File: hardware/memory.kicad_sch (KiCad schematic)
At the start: 0 parts

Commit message: Emulated memory: rewrite architecture, add local-bus/register sheet
- docs/v3-architecture.md: RP2350B serves DCK/ROM images from internal SRAM
  via PIO+DMA; no flash or SRAM chips; 8-bit multiplexed local bus; slot map
  file replaces fixed flash banks; ESP32-C3-WROOM-02 for Zimodem.
- memory sheet: 74LVC257 address byte muxes, ALO/AHI/CTL/STAT registers,
  74LVC139 select, power-on clear for CTL.
- interface sheet: 74LVC06 inverting open-drain drivers with active-high
  requests (safe power-up state), RESET_HOLD pull-up, address transceivers
  always enabled, MA8-MA15 to the muxes, WIFI_DL inverter.
- ERC: only cross-sheet labels/inputs pending the MCU and peripheral sheets.

Co-Authored-By: Claude Fable 5.1 <noreply@anthropic.com>
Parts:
- added C10, C11, C12, C13, C14, C15, C16: 100n, Capacitor_SMD:C_0603_1608Metric, symbol Device:C
- added C9: 1u, Capacitor_SMD:C_0603_1608Metric, symbol Device:C
- added D1: BAT54, Diode_SMD:D_SOD-123, symbol Device:D_Schottky
- added R4: 10k, Resistor_SMD:R_0603_1608Metric, symbol Device:R
- added U10, U11: 74LVC257APW, Package_SO:TSSOP-16_4.4x5mm_P0.65mm, symbol 74xx:74LS257
- added U12, U13: 74LVC574APW, Package_SO:TSSOP-20_4.4x6.5mm_P0.65mm, symbol 74xx:74LS574
- added U14: 74LVC273APW, Package_SO:TSSOP-20_4.4x6.5mm_P0.65mm, symbol 74xx:74LS273
- added U15: 74LVC541APW, Package_SO:TSSOP-20_4.4x6.5mm_P0.65mm, symbol 74xx:74LS541
- added U16: 74LVC139APW, Package_SO:TSSOP-16_4.4x5mm_P0.65mm, symbol 74xx:74LS139
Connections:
- new net +3V3: C10.1, C11.1, C12.1, C13.1, C14.1, C15.1, C16.1, D1.2 (A), R4.1, U10.16 (VCC), U11.16 (VCC), U12.20 (VCC), U13.20 (VCC), U14.20 (VCC), U15.20 (VCC), U16.15 (E), U16.16 (VCC)
- new net ASEL: U10.1 (S), U11.1 (S)
- new net BUSRQ: U14.5 (Q1)
- new net DMA_EN: U14.2 (Q0)
- new net GND: C10.2, C11.2, C12.2, C13.2, C14.2, C15.2, C16.2, C9.2, U10.8 (GND), U11.8 (GND), U12.10 (GND), U13.10 (GND), U14.10 (GND), U15.10 (GND), U15.19 (G2), U16.13 (A1), U16.14 (A0), U16.8 (GND)
- new net JOY_DOWN: U15.3 (A1)
- new net JOY_FIRE1: U15.6 (A4)
- new net JOY_FIRE2: U15.7 (A5)
- new net JOY_LEFT: U15.4 (A2)
- new net JOY_RIGHT: U15.5 (A3)
- new net JOY_UP: U15.2 (A0)
- new net LED: U14.16 (Q6)
- new net MA0: U10.2 (I0a), U12.19 (Q0)
- new net MA1: U10.5 (I0b), U12.18 (Q1)
- new net MA10: U10.13 (I1c), U13.17 (Q2)
- new net MA11: U10.10 (I1d), U13.16 (Q3)
- new net MA12: U11.3 (I1a), U13.15 (Q4)
- new net MA13: U11.6 (I1b), U13.14 (Q5)
- new net MA14: U11.13 (I1c), U13.13 (Q6)
- new net MA15: U11.10 (I1d), U13.12 (Q7)
- new net MA2: U10.14 (I0c), U12.17 (Q2)
- new net MA3: U10.11 (I0d), U12.16 (Q3)
- new net MA4: U11.2 (I0a), U12.15 (Q4)
- new net MA5: U11.5 (I0b), U12.14 (Q5)
- new net MA6: U11.14 (I0c), U12.13 (Q6)
- new net MA7: U11.11 (I0d), U12.12 (Q7)
- new net MA8: U10.3 (I1a), U13.19 (Q0)
- new net MA9: U10.6 (I1b), U13.18 (Q1)
- new net MD0: U10.4 (Za), U12.2 (D0), U13.2 (D0), U14.3 (D0), U15.18 (Y0)
- new net MD1: U10.7 (Zb), U12.3 (D1), U13.3 (D1), U14.4 (D1), U15.17 (Y1)
- new net MD2: U10.12 (Zc), U12.4 (D2), U13.4 (D2), U14.7 (D2), U15.16 (Y2)
- new net MD3: U10.9 (Zd), U12.5 (D3), U13.5 (D3), U14.8 (D3), U15.15 (Y3)
- new net MD4: U11.4 (Za), U12.6 (D4), U13.6 (D4), U14.13 (D4), U15.14 (Y4)
- new net MD5: U11.7 (Zb), U12.7 (D5), U13.7 (D5), U14.14 (D5), U15.13 (Y5)
- new net MD6: U11.12 (Zc), U12.8 (D6), U13.8 (D6), U14.17 (D6), U15.12 (Y6)
- new net MD7: U11.9 (Zd), U12.9 (D7), U13.9 (D7), U14.18 (D7), U15.11 (Y7)
- new net NMI_REQ: U14.6 (Q2)
- new net REG_SEL0: U16.2 (A0)
- new net REG_SEL1: U16.3 (A1)
- new net SD_CD: U15.9 (A7)
- new net WIFI_DL: U14.15 (Q5)
- new net WIFI_EN: U14.12 (Q4)
- new net nAOE: U10.15 (OE), U11.15 (OE)
- new net nBUSAK: U15.8 (A6)
- new net nDMA_EN: U12.1 (OE), U13.1 (OE)
- new net nOLED_RST: U14.9 (Q3)
- new net nPOR: C9.1, D1.1 (K), R4.2, U14.1 (~{Mr})
- new net nRD_STAT: U15.1 (G1), U16.7 (O3)
- new net nREG_STB: U16.1 (E)
- new net nWR_AHI: U13.11 (Cp), U16.5 (O1)
- new net nWR_ALO: U12.11 (Cp), U16.4 (O0)
- new net nWR_CTL: U14.11 (Cp), U16.6 (O2)
- no-connect marks 0 -> 5
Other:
- note added: "Local bus MD0-MD7 carries the Z80 address (two bytes through U10/U11), the Z80 data (interface sheet U3) and the registers."
- note added: "No flash or SRAM: the RP2350B serves memory from internal SRAM (PIO + DMA). ALO/AHI drive MA only in DMA mode."
- note added: "R4/C9/D1: ~10 ms power-on clear of CTL,"
- note added: "so all control bits start at 0."
- note removed: "Flash (TSOP-32), SRAM (SOP-32), ALO/AHI/CTL/STAT registers, 74LVC139, 74LVC157, 74LVC125 DMA drivers"
- title: TS-Pico v3: Memory Bus -> TS-Pico v3: Local Bus and Registers

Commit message: Remaining sheets: power, SD and display, WiFi, audio, joystick; ERC clean
- Power: Schottky diode-OR of edge +5V and USB VBUS (card runs from the
  2068/expansion bus, USB alone, or both), two TLV1117LV33 LDOs, bulk caps
- SD: Hirose DM3AT in SPI mode with series R, pull-ups, card detect to STAT
- OLED: 7-pin header (Waveshare 1.27in 128x96 SSD1351) on SPI1
- WiFi: ESP32-C3-WROOM-02 on UART, EN/boot from CTL, IO8 pull-up
- Audio: PWM low-pass, 2068 SOUND mix, MCP6002 buffers, 3.5 mm jack
- Joystick: DE-9 Kempston with pull-ups, series R, optional +5V jumper
- Memory sheet: activity LED on CTL bit 6
- Docs: power decision updated

Co-Authored-By: Claude Fable 5.1 <noreply@anthropic.com>
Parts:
- added D4: green, LED_SMD:LED_0603_1608Metric, symbol Device:LED
- added R5: 1k, Resistor_SMD:R_0603_1608Metric, symbol Device:R
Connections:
- net GND: now also D4.1 (K)
- net LED: now also R5.1
- new net LED_K: D4.2 (A), R5.2
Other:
- note added: "R5/D4: activity LED, CTL bit 6."
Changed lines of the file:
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@@
   (text "R4/C9/D1: ~10 ms power-on clear of CTL," (exclude_from_sim no) (at 355 118 0) (effects (font (size 1.5 1.5)) (justify left bottom)))
   (text "so all control bits start at 0." (exclude_from_sim no) (at 355 121 0) (effects (font (size 1.5 1.5)) (justify left bottom)))
+  (symbol (lib_id "Device:R") (at 369.57 160.02 0) (unit 1)
+    (exclude_from_sim no) (in_bom yes) (on_board yes) (dnp no)
+    (property "Reference" "R5" (at 372.57 151.71 0) (effects (font (size 1.27 1.27)) (justify left)))
+    (property "Value" "1k" (at 372.57 154.21 0) (effects (font (size 1.27 1.27)) (justify left)))
+    (property "Footprint" "Resistor_SMD:R_0603_1608Metric" (at 369.57 160.02 0) (effects (font (size 1.27 1.27)) (justify left) (hide yes)))
+    (property "Datasheet" "" (at 369.57 160.02 0) (effects (font (size 1.27 1.27)) (justify left) (hide yes)))
+    (property "Description" "" (at 369.57 160.02 0) (effects (font (size 1.27 1.27)) (justify left) (hide yes)))
+    (pin "1")
+    (pin "2")
+    (instances (project "tspico-v3" (path "/9088d141-8624-4d5c-91a9-7a3a7a90b3cc/e99fe9a8-9037-4040-a342-12a0ddc42052" (reference "R5") (unit 1))))
+  )
+  (global_label "LED" (shape input) (at 369.57 156.21 90) (effects (font (size 1.27 1.27)) (justify left)))
+  (label "LED_K" (at 369.57 163.83 270) (effects (font (size 1.27 1.27)) (justify right bottom)))
+  (symbol (lib_id "Device:LED") (at 374.65 180.34 0) (unit 1)
+    (exclude_from_sim no) (in_bom yes) (on_board yes) (dnp no)
+    (property "Reference" "D4" (at 377.65 173.3 0) (effects (font (size 1.27 1.27)) (justify left)))
+    (property "Value" "green" (at 377.65 175.8 0) (effects (font (size 1.27 1.27)) (justify left)))
+    (property "Footprint" "LED_SMD:LED_0603_1608Metric" (at 374.65 180.34 0) (effects (font (size 1.27 1.27)) (justify left) (hide yes)))
+    (property "Datasheet" "" (at 374.65 180.34 0) (effects (font (size 1.27 1.27)) (justify left) (hide yes)))
+    (property "Description" "" (at 374.65 180.34 0) (effects (font (size 1.27 1.27)) (justify left) (hide yes)))
+    (pin "1")
+    (pin "2")
+    (instances (project "tspico-v3" (path "/9088d141-8624-4d5c-91a9-7a3a7a90b3cc/e99fe9a8-9037-4040-a342-12a0ddc42052" (reference "D4") (unit 1))))
+  )
+  (label "LED_K" (at 378.46 180.34 0) (effects (font (size 1.27 1.27)) (justify left bottom)))
+  (label "GND" (at 370.84 180.34 180) (effects (font (size 1.27 1.27)) (justify right bottom)))
+  (text "R5/D4: activity LED, CTL bit 6." (exclude_from_sim no) (at 355 195 0) (effects (font (size 1.5 1.5)) (justify left bottom)))
   (symbol (lib_id "Device:C") (at 39.37 255.27 0) (unit 1)
     (exclude_from_sim no) (in_bom yes) (on_board yes) (dnp no)

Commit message: BOM pass: LCSC and MPN fields on every part, JLCPCB BOM export
- scripts/parts.py: part table looked up 2026-09-16; schlib stamps fields
- substitutions for stock: 74HC273PW, 74LVC139PW, TI LVC04/08/126/574/1G86,
  33R USB series, XKB TS-1187A switches, Panasonic polymer 220uF, B5819W
- bom/: JLCPCB-format and full BOM CSVs

Co-Authored-By: Claude Fable 5.1 <noreply@anthropic.com>
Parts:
- C10, C11, C12, C13, C14, C15, C16: LCSC (none) -> C14663; MPN (none) -> CC0603KRX7R9BB104
- C9: LCSC (none) -> C15849; MPN (none) -> CL10A105KB8NNNC
- D1: value BAT54 -> B5819W; LCSC (none) -> C8598; MPN (none) -> B5819W SL
- D4: LCSC (none) -> C72043; MPN (none) -> 19-217/GHC-YR1S2/3T
- R4: LCSC (none) -> C25804; MPN (none) -> 0603WAF1002T5E
- R5: LCSC (none) -> C21190; MPN (none) -> 0603WAF1001T5E
- U10, U11: LCSC (none) -> C6083; MPN (none) -> 74LVC257APW,118
- U12, U13: LCSC (none) -> C7672; MPN (none) -> SN74LVC574APWR
- U14: value 74LVC273APW -> 74HC273PW; LCSC (none) -> C131680; MPN (none) -> 74HC273PW,118
- U15: LCSC (none) -> C6093; MPN (none) -> 74LVC541APW,118
- U16: value 74LVC139APW -> 74LVC139PW; LCSC (none) -> C6064; MPN (none) -> 74LVC139PW,118

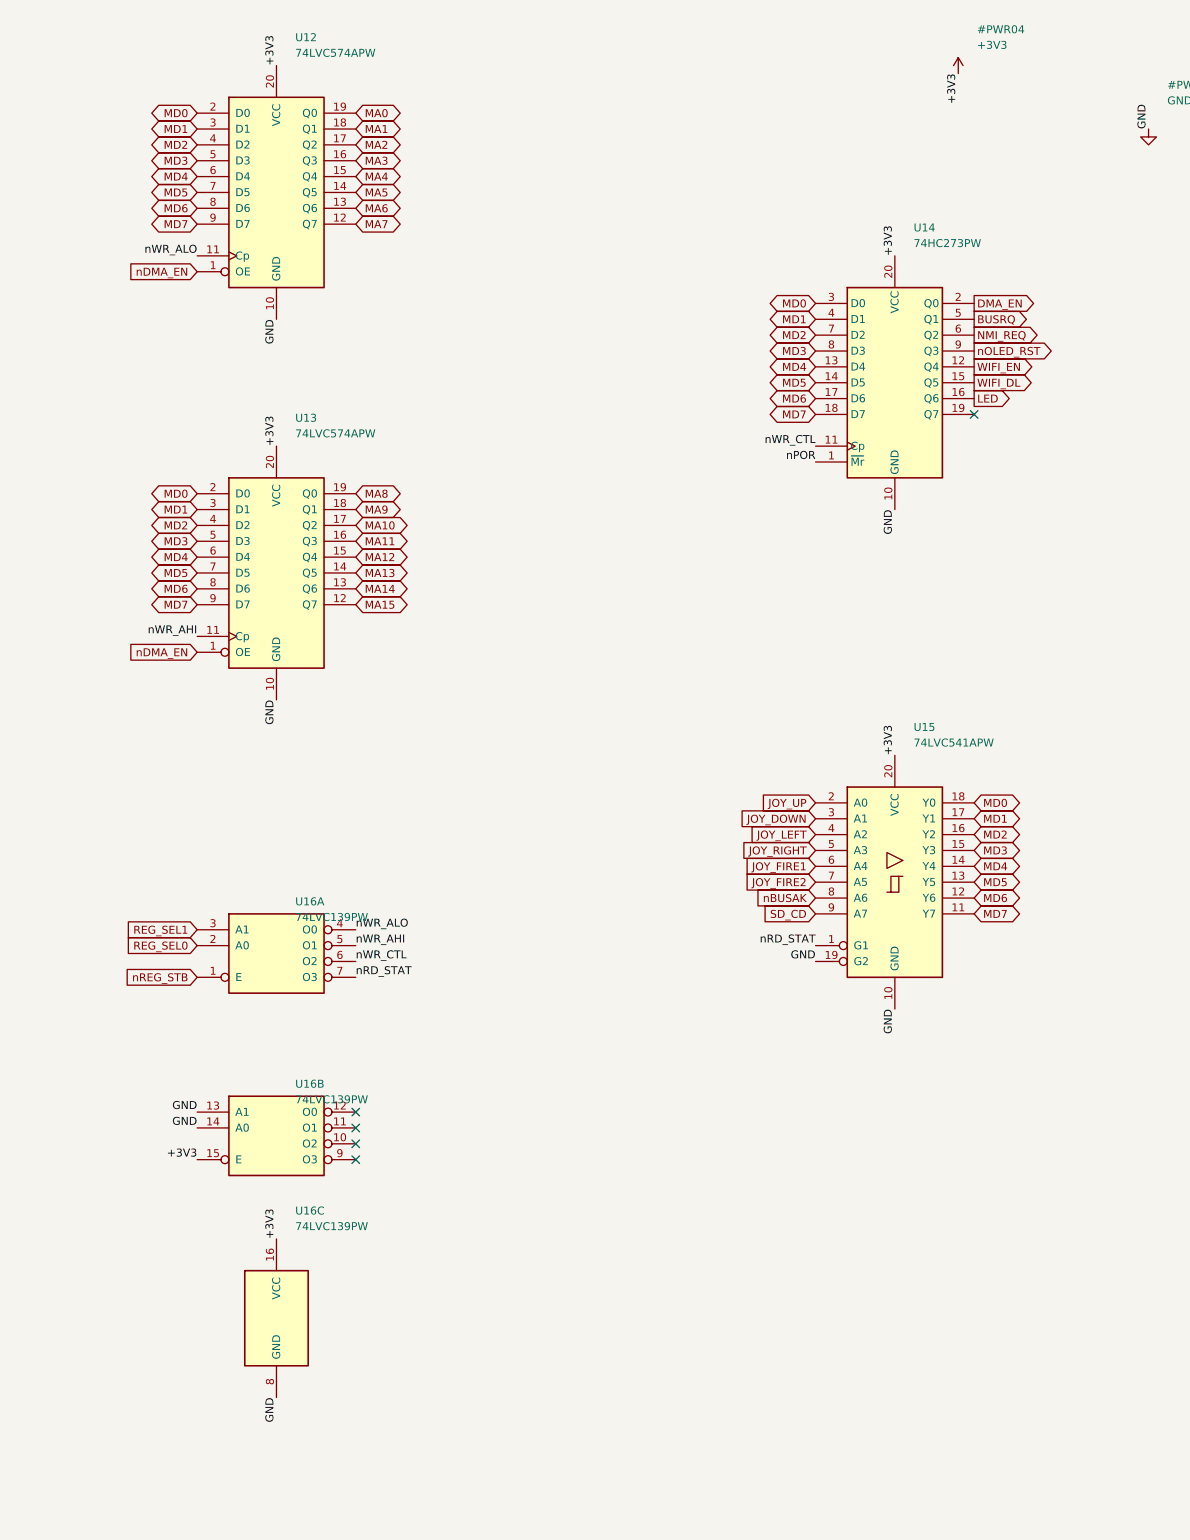
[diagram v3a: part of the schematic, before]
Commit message: BOM cost optimisation against the JLCPCB catalog; schematic-side regulator fix
jlc_price.py prices the BOM via JLCPCB's parts API. Substitutions cut parts+fees
per board from $32.95 to $17.19 on a 10-board run: PSRAM DNP, electrolytic bulk
caps, TF-01A socket, PJ-320D jack, 74HC574, GD25Q128E, 0603 10 uF, basic LED,
preferred MCP6002; U16 decoder deleted (strobes on GPIO), U8 and U15 become
74LVC245s; J3/J5 hand-soldered. Adds the AOTA inductor and VREG_AVDD filter.
PCB needs a relayout; fab/ is stale.

Co-Authored-By: Claude Fable 5.1 <noreply@anthropic.com>
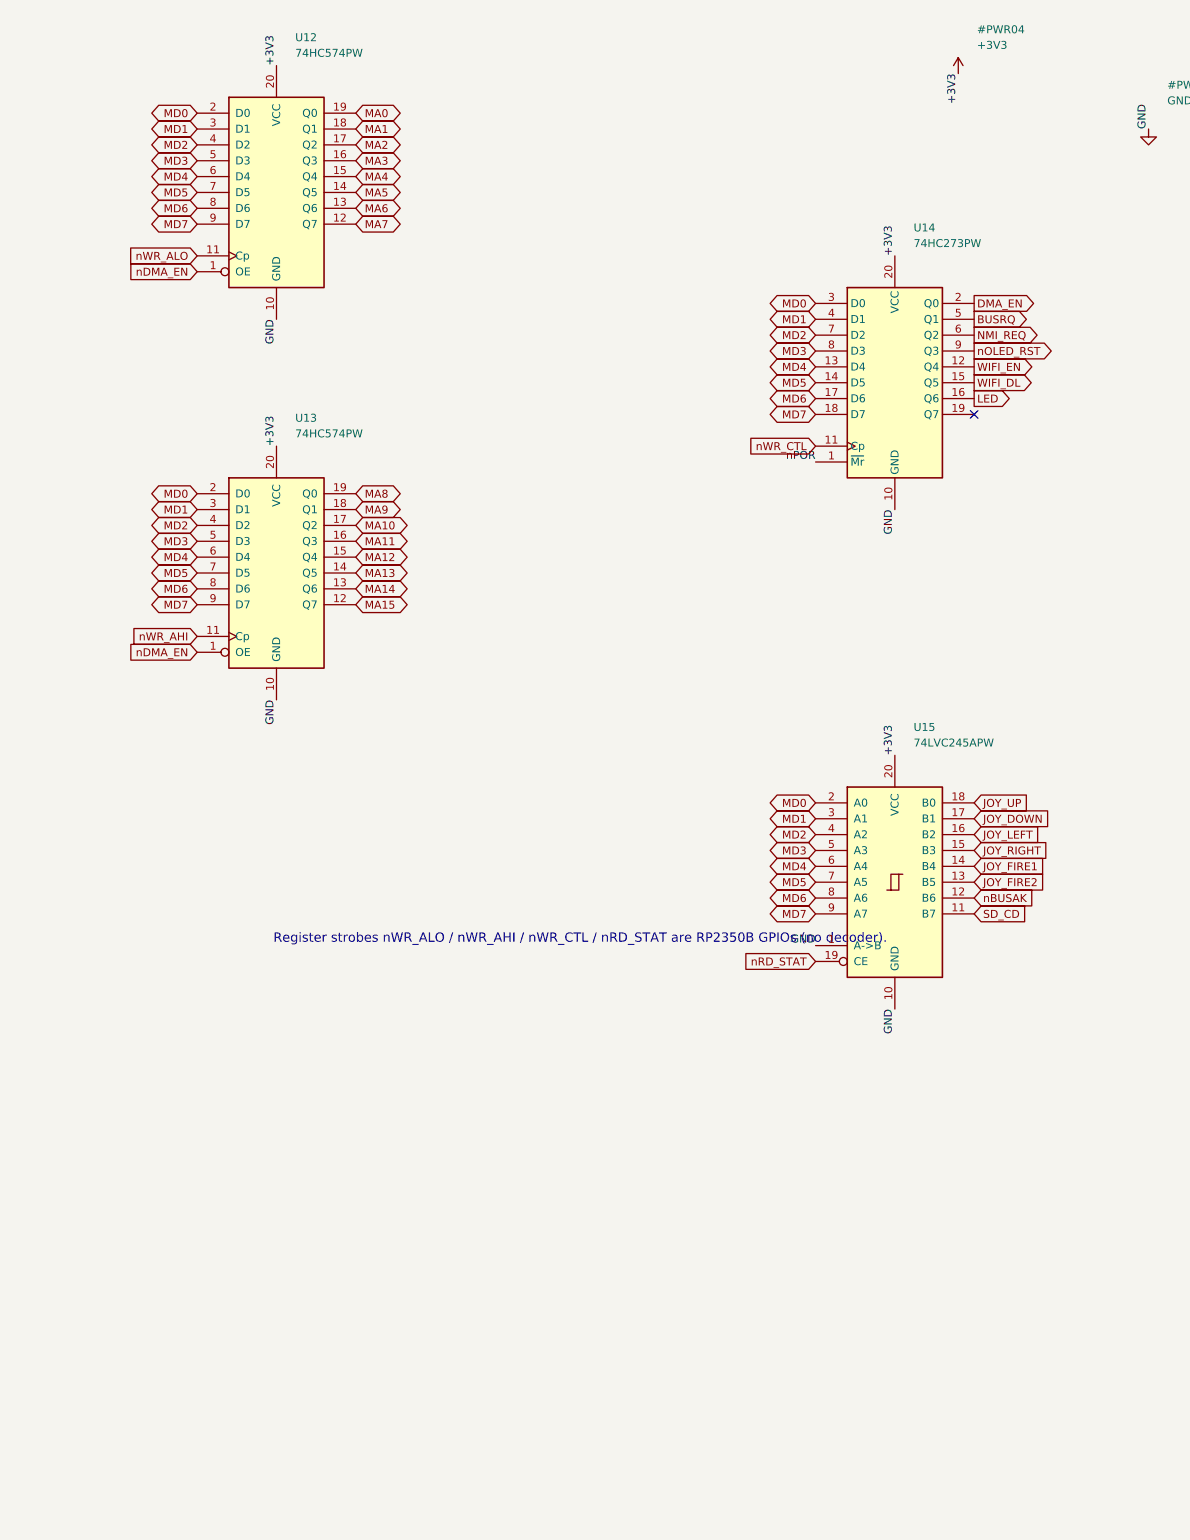
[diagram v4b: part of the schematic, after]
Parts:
- removed U15: 74LVC541APW, Package_SO:TSSOP-20_4.4x6.5mm_P0.65mm, symbol 74xx:74LS541
- removed U16: 74LVC139PW, Package_SO:TSSOP-16_4.4x5mm_P0.65mm, symbol 74xx:74LS139
- added U15: 74LVC245APW, Package_SO:TSSOP-20_4.4x6.5mm_P0.65mm, symbol 74xx:74LS245
- D4: footprint LED_SMD:LED_0603_1608Metric -> LED_SMD:LED_0805_2012Metric; LCSC C72043 -> C2297; MPN 19-217/GHC-YR1S2/3T -> KT-0805G
- U10, U11: LCSC C6083 -> C205921; MPN 74LVC257APW,118 -> SN74LVC257APWR
- U12, U13: value 74LVC574APW -> 74HC574PW; LCSC C7672 -> C54796860; MPN SN74LVC574APWR -> 74HC574PW
- U14: LCSC C131680 -> C44512760; MPN 74HC273PW,118 -> SN74HC273PWR-JSM
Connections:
- net +3V3: now also U15.20 (VCC)
- net GND: now also U15.1 (A->B), U15.10 (GND)
- net JOY_DOWN: now also U15.17 (B1)
- net JOY_FIRE1: now also U15.14 (B4)
- net JOY_FIRE2: now also U15.13 (B5)
- net JOY_LEFT: now also U15.16 (B2)
- net JOY_RIGHT: now also U15.15 (B3)
- net JOY_UP: now also U15.18 (B0)
- net MD0: now also U15.2 (A0)
- net MD1: now also U15.3 (A1)
- net MD2: now also U15.4 (A2)
- net MD3: now also U15.5 (A3)
- net MD4: now also U15.6 (A4)
- net MD5: now also U15.7 (A5)
- net MD6: now also U15.8 (A6)
- net MD7: now also U15.9 (A7)
- net SD_CD: now also U15.11 (B7)
- net nBUSAK: now also U15.12 (B6)
- net nRD_STAT: now also U15.19 (CE)
- no-connect marks 5 -> 1
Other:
- note added: "Register strobes nWR_ALO / nWR_AHI / nWR_CTL / nRD_STAT are RP2350B GPIOs (no decoder)."

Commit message: Logic consolidation: 15 packages to 8 fitted
Address buffers' output enables replace the 74LVC257 byte muxes and the MA bus;
one 74LVC32 makes MEMRD/MEMWR/IORD/IOWR strobes (replaces the 04 and 08);
XL9555 I2C expander replaces the CTL register, its power-on clear and the STAT
buffer; DMA parts are a DNP stuffing option (config.DMA_OPTION), with 74LVC574
latches directly on the address bus. GPIO map, architecture doc and cost notes
updated. Parts + fees per board now $14.93 on a 10-board run.

Co-Authored-By: Claude Fable 5.1 <noreply@anthropic.com>
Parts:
- removed C11, C12, C13, C14, C15, C16: 100n, Capacitor_SMD:C_0603_1608Metric, symbol Device:C
- removed C9: 1u, Capacitor_SMD:C_0603_1608Metric, symbol Device:C
- removed D1: B5819W, Diode_SMD:D_SOD-123, symbol Device:D_Schottky
- removed R4: 10k, Resistor_SMD:R_0603_1608Metric, symbol Device:R
- removed U10, U11: 74LVC257APW, Package_SO:TSSOP-16_4.4x5mm_P0.65mm, symbol 74xx:74LS257
- removed U12, U13: 74HC574PW, Package_SO:TSSOP-20_4.4x6.5mm_P0.65mm, symbol 74xx:74LS574
- removed U14: 74HC273PW, Package_SO:TSSOP-20_4.4x6.5mm_P0.65mm, symbol 74xx:74LS273
- removed U15: 74LVC245APW, Package_SO:TSSOP-20_4.4x6.5mm_P0.65mm, symbol 74xx:74LS245
- added R10, R11, R12, R13, R8, R9: 10k, Resistor_SMD:R_0603_1608Metric, symbol Device:R
- added R6, R7: 4k7, Resistor_SMD:R_0603_1608Metric, symbol Device:R
- added U15: XL9555, Package_SO:TSSOP-24_4.4x7.8mm_P0.65mm, symbol Interface_Expansion:PCA9555PW
- R5: value 1k -> 100; LCSC C21190 -> C22775; MPN 0603WAF1001T5E -> 0603WAF1000T5E
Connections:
- net LED is gone; now on net +3V3: R5.1
- net +3V3: now also R6.1, R7.1, R8.1, U15.24 (VDD)
- net BUSRQ: now also R9.1, U15.4 (IO0_0)
- net GND: now also R10.2, R11.2, R12.2, R13.2, R9.2, U15.12 (VSS), U15.2 (A1), U15.21 (A0), U15.3 (A2); no longer D4.1 (K)
- net JOY_DOWN: now also U15.14 (IO1_1)
- net JOY_FIRE1: now also U15.17 (IO1_4)
- net JOY_FIRE2: now also U15.18 (IO1_5)
- net JOY_LEFT: now also U15.15 (IO1_2)
- net JOY_RIGHT: now also U15.16 (IO1_3)
- net JOY_UP: now also U15.13 (IO1_0)
- net NMI_REQ: now also R10.1, U15.5 (IO0_1)
- net SD_CD: now also U15.20 (IO1_7)
- net WIFI_DL: now also R13.1, U15.8 (IO0_4)
- net WIFI_EN: now also R12.1, U15.7 (IO0_3)
- net nOLED_RST: now also R11.1, U15.6 (IO0_2)
- net LED_K renamed LED_A
- new net I2C_SCL: R7.2, U15.22 (SCL)
- new net I2C_SDA: R6.2, U15.23 (SDA)
- new net nBUSAK_L: U15.19 (IO1_6)
- new net nIOX_INT: R8.2, U15.1 (~{INT})
- new net nLED: D4.1 (K), U15.9 (IO0_5)
- no-connect marks 1 -> 2
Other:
- note added: "No flash or SRAM: the RP2350B serves memory from internal SRAM (PIO + DMA)."
- note added: "R5/D4: activity LED, on when nLED is driven low."
- note added: "R9-R13: 10 k pull-downs beat the expander's 100 k pull-ups until the firmware configures the port."
- note added: "Slow control and status on one I2C expander. The fast local bus MD0-MD7 (address groups, Z80 data) is on the interface sheet."
- note removed: "Local bus MD0-MD7 carries the Z80 address (two bytes through U10/U11), the Z80 data (interface sheet U3) and the registers."
- note removed: "No flash or SRAM: the RP2350B serves memory from internal SRAM (PIO + DMA). ALO/AHI drive MA only in DMA mode."
- note removed: "R4/C9/D1: ~10 ms power-on clear of CTL,"
- note removed: "R5/D4: activity LED, CTL bit 6."
- note removed: "Register strobes nWR_ALO / nWR_AHI / nWR_CTL / nRD_STAT are RP2350B GPIOs (no decoder)."
- note removed: "so all control bits start at 0."
- title: TS-Pico v3: Local Bus and Registers -> TS-Pico v3: I/O Expander
